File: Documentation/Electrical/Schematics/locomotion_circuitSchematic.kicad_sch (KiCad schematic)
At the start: 6 parts

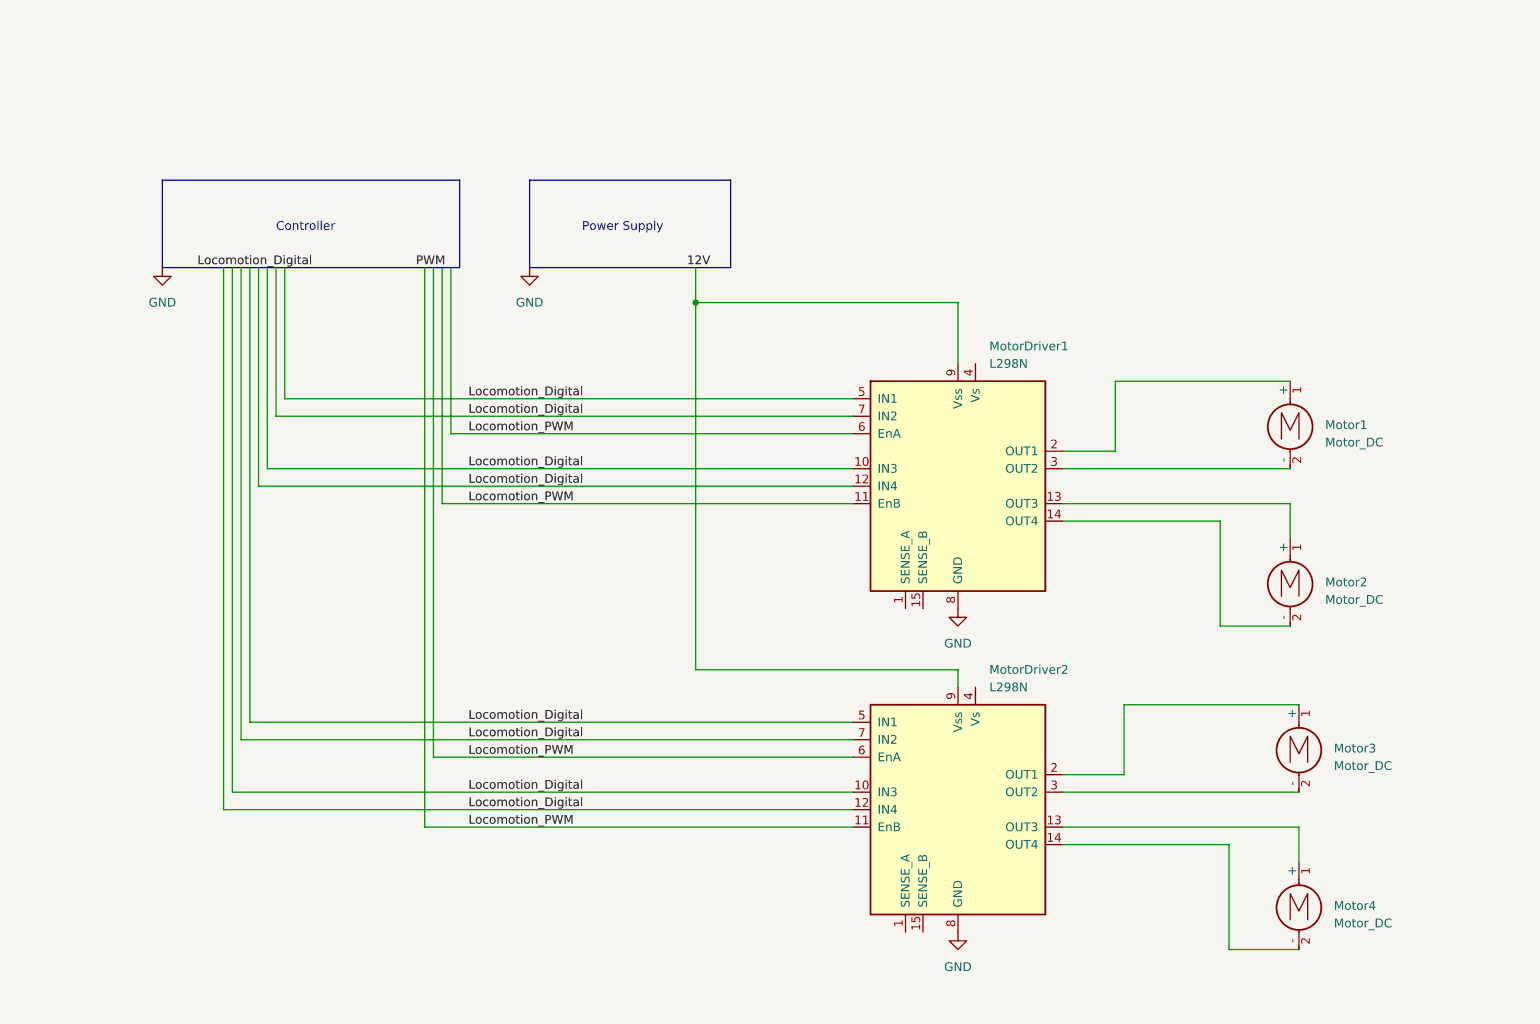
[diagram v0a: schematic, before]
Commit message: updated circuit schematic
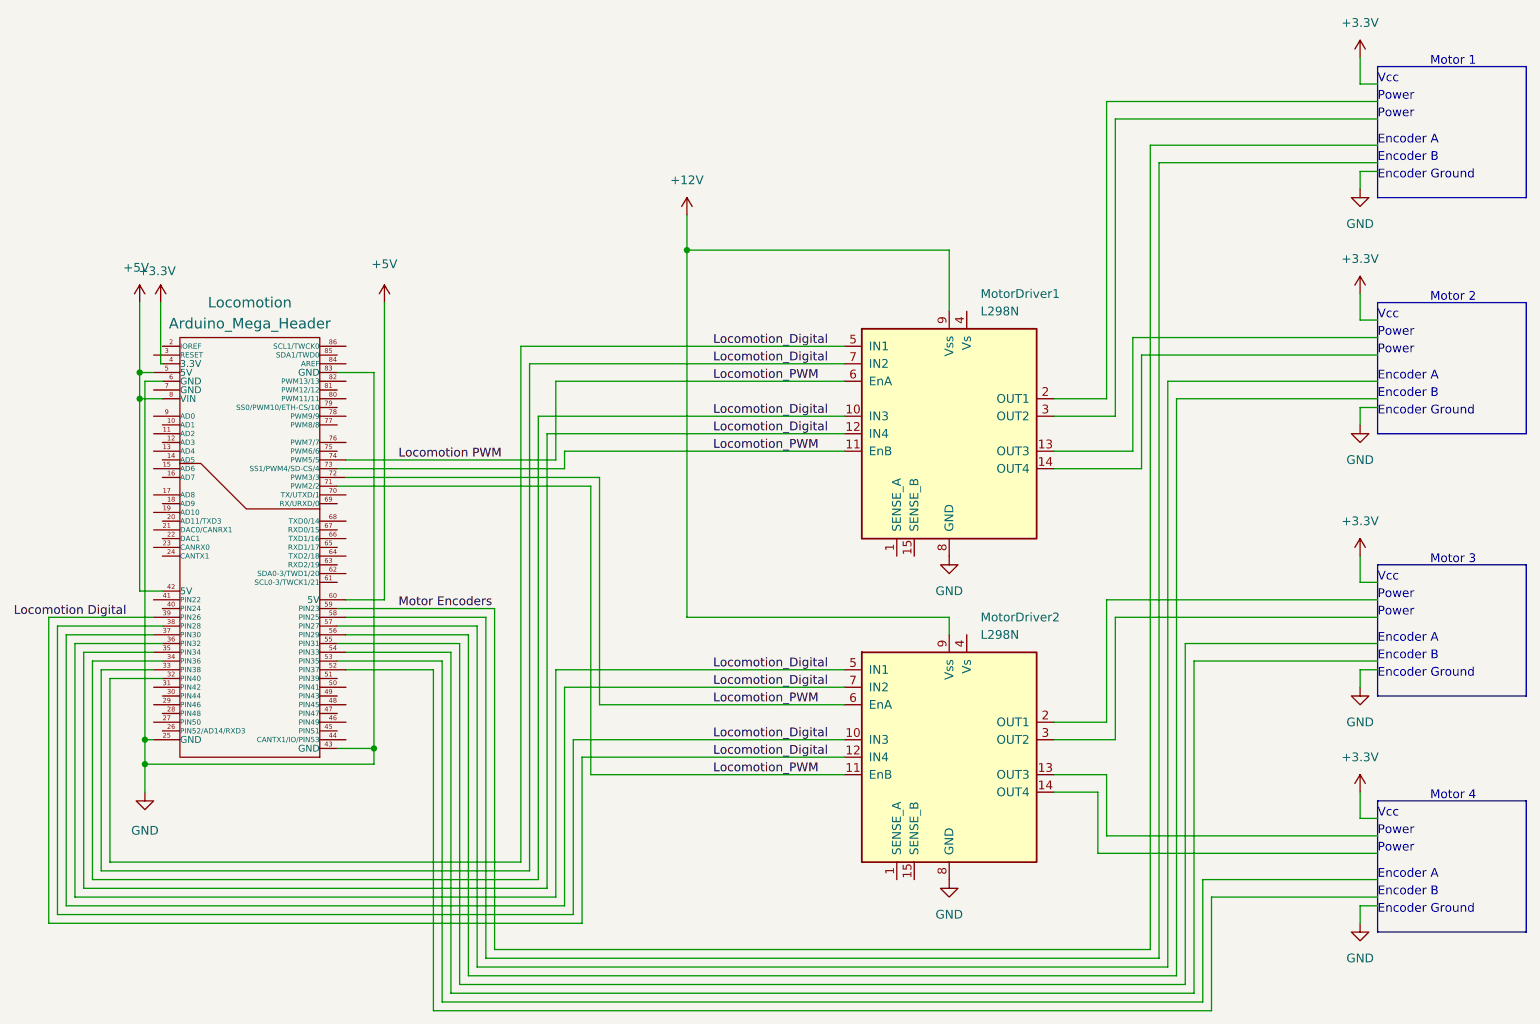
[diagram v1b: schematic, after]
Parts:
- removed Motor1, Motor2, Motor3, Motor4: Motor_DC, symbol Motor:Motor_DC
- added Locomotion: Arduino_Mega_Header, symbol w_connectors:Arduino_Mega_Header
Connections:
- net GND: now also Locomotion.25 (GND), Locomotion.43 (GND), Locomotion.6 (GND), Locomotion.83 (GND)
- net Locomotion_Digital: now also Locomotion.32 (PIN40), Locomotion.33 (PIN38), Locomotion.34 (PIN36), Locomotion.35 (PIN34), Locomotion.36 (PIN32), Locomotion.37 (PIN30), Locomotion.38 (PIN28), Locomotion.39 (PIN26)
- net +12V: now reaches MotorDriver1.9 (Vss), MotorDriver2.9 (Vss)
- net Locomotion_PWM renamed Locomotion PWM
- net Locomotion PWM: now also Locomotion.71 (PWM2/2), Locomotion.72 (PWM3/3), Locomotion.73 (SS1/PWM4/SD-CS/4), Locomotion.74 (PWM5/5)
- new net +3V3: Locomotion.4 (3.3V)
- new net +5V: Locomotion.42 (5V), Locomotion.5 (5V), Locomotion.60 (5V), Locomotion.8 (VIN)
- new net Motor Encoders: Locomotion.59 (PIN23)
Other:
- note added: "Encoder A"
- note added: "Encoder B"
- note added: "Encoder Ground"
- note added: "Motor 1"
- note added: "Motor 2"
- note added: "Motor 3"
- note added: "Motor 4"
- note added: "Power"
- note added: "Vcc"
- note removed: "Controller"
- note removed: "Power Supply"
- moved on the sheet: MotorDriver1, MotorDriver2
